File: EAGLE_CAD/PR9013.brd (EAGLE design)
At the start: 70.1 x 70.1 mm, 55 parts, among them J1 M3_SCREW_POST, SW1 SPST_TACT-KMR2, Y1 32.768kHz

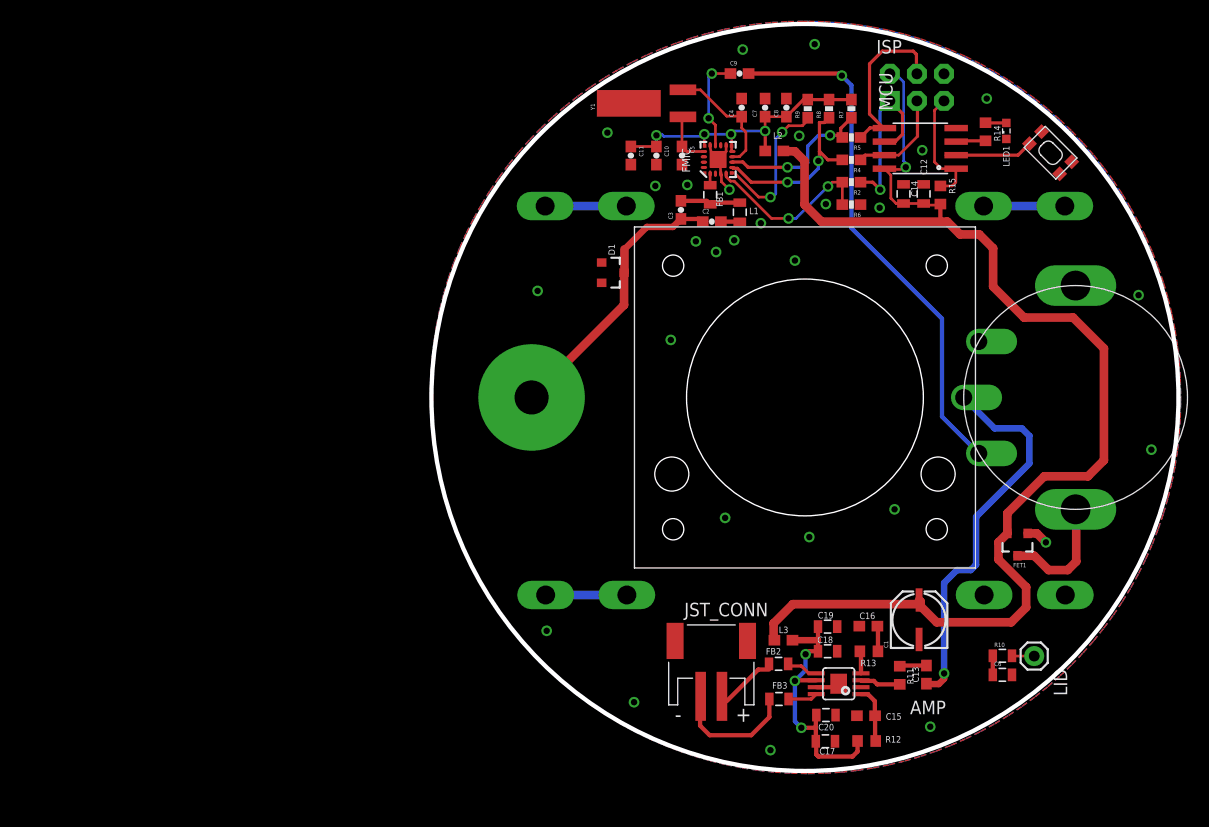
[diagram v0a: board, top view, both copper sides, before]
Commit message: Some significant fixes & changes
So i started by looking at the alignment of the board, speaker, pot &
antenna. it turns out these were all a bit wacky - all laid out at
different grid spacings and none of them consistent. the alignment of
all was off relative to one another, and the board itself was just at
some arbitrary location. so:

i moved the whole board so that it’s centered at 35mm x 35mm
moved the speaker so it’s centered at 35mm x 35mm
moved the antenna and pot so they’re centered at 35mm (Ydim) and are
each 25.5mm from centerline in the Xdim
moved the batteries so that they’re centered at 35mm (Xdim) and each
18.5mm from centerline in the Ydim

then i:
added a wire for the batteries on the left side. i’d like to modify
this but it’s a start.
added bRestrict circles for the four bolts for the speaker. these are
just over 5mm in diameter, so they’re just a little bigger than our
nuts will be. there should be NO TRACES IN THESE ZONES!!!

i did *NOT* remove all the traces in those bRestricts, though - i need
to do other stuff at the moment.

there MAY BE SOME OTHER CHANGES NECESSARY as a result of my
modifications. i wanted to get all the mechanical components 100% set
and locked, so that’s all i’m sure of at the minute.
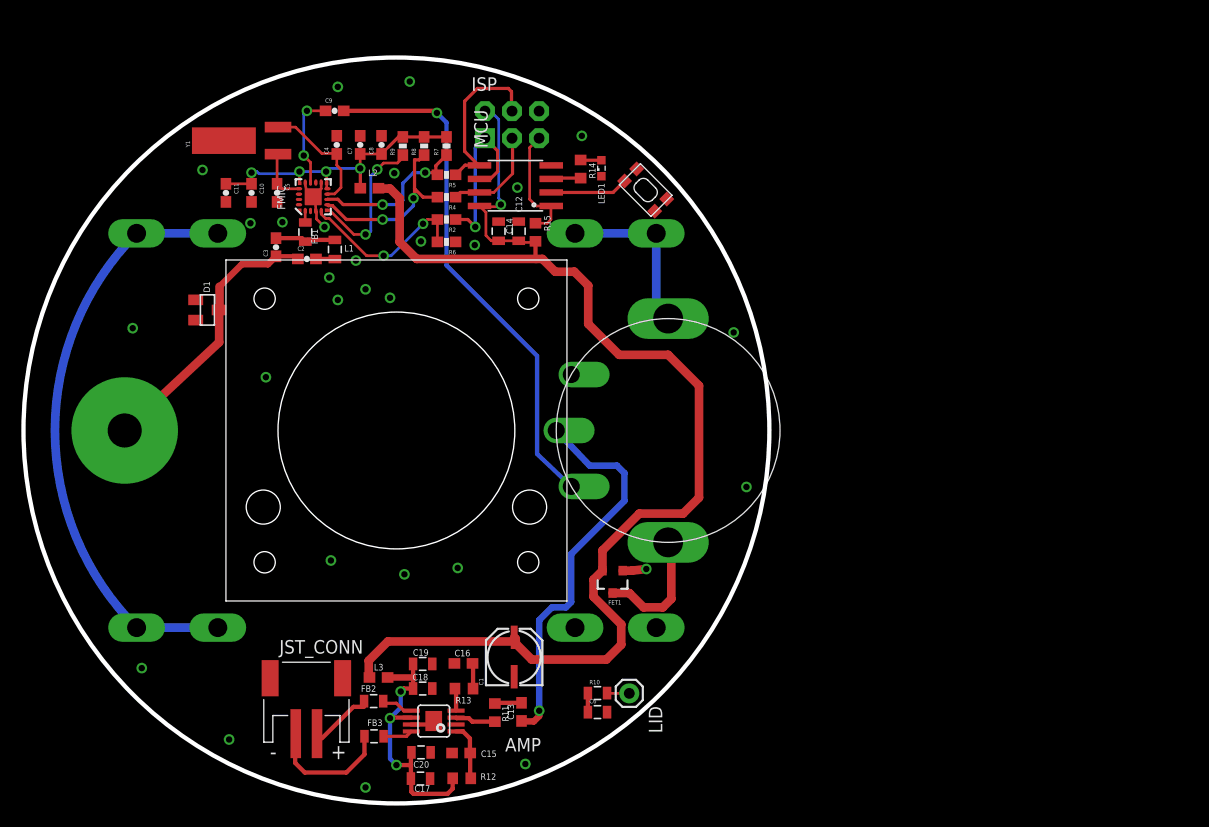
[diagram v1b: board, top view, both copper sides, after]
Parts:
- D1: device SparkFun-DiscreteSemi:SOT23-3 -> SparkFun-DiscreteSemi:SOT23
- moved JP6 38.5 mm to (35.0, 16.5)
- moved SPEAKER 38.5 mm to (35.0, 35.0)
- moved JP5 38.4 mm to (35.0, 53.5)
- moved R1 38.4 mm to (60.5, 35.0)
- moved J1 38.3 mm to (9.50, 35.0)
- moved C1 38.2 mm to (45.9, 13.7)
- moved C17 38.2 mm to (37.3, 2.33)
- moved C4 38.2 mm to (29.4, 61.8)
- moved FB2 38.2 mm to (32.9, 9.60)
- moved FB3 38.2 mm to (32.9, 6.30)
- moved AMP 38.2 mm to (38.5, 7.73)
- moved C10 38.2 mm to (21.4, 57.3)
- moved C11 38.2 mm to (19.0, 57.3)
- moved C12 38.2 mm to (46.5, 53.7)
- moved C14 38.2 mm to (44.6, 53.7)
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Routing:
- net N$13: track 15.2 -> 52.2 mm
- net N$15: track 7.62 -> 16.1 mm
- added copper zone on layer 16, net N$21
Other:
- board size 70.1 x 70.1 mm -> 70 x 70 mm

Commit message: moved some traces
redid left battery trace
redid the traces that were violating brestrict near the speaker
moved the lid connection off the board - think we’ll prob move that to
the speaker screws
moved other traces in small ways
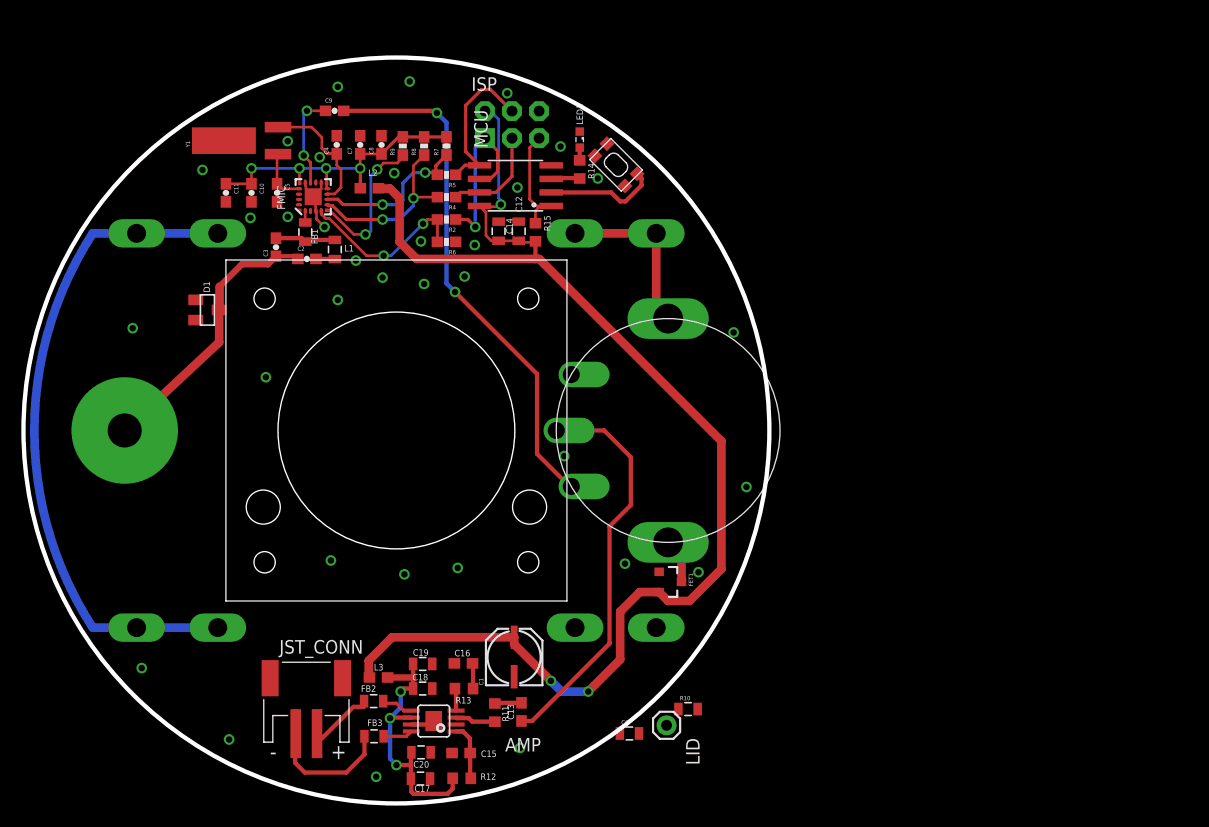
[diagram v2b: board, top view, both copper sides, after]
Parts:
- moved R10 8.63 mm to (62.4, 8.85)
- moved FET1 5.37 mm to (60.7, 20.8), turned to 270 degrees
- moved LID 4.61 mm to (60.4, 7.33)
- moved SW1 3.65 mm to (55.6, 59.9), turned to 315 degrees
- moved C6 3.61 mm to (56.9, 6.57)
- moved LED1 3.37 mm to (52.2, 62.3), turned to 270 degrees
- moved R14 0.10 mm to (52.2, 59.5)
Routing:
- net N$13: track 52.2 -> 60.5 mm
- net N$34: track 11.8 -> 4.23 mm
- net N$11: track 8.30 -> 11.7 mm
- net GND: track 13.6 -> 11.3 mm, vias 28 -> 34
- net N$8: track 2.10 -> 0.00 mm
- net N$35: track 1.79 -> 0.00 mm
- net SDIO: track 16.1 -> 14.6 mm
- net PB5: track 11.3 -> 10.2 mm
- net A_OUT: track 36.9 -> 37.6 mm, vias 1 -> 0
- net N$7: track 1.96 -> 1.20 mm
- net 3.3V: track 28.7 -> 29.4 mm
- net N$1: track 11.4 -> 12.0 mm
- net VCC: track 123.6 -> 124.1 mm, vias 1 -> 3
- net A_IN: vias 1 -> 2

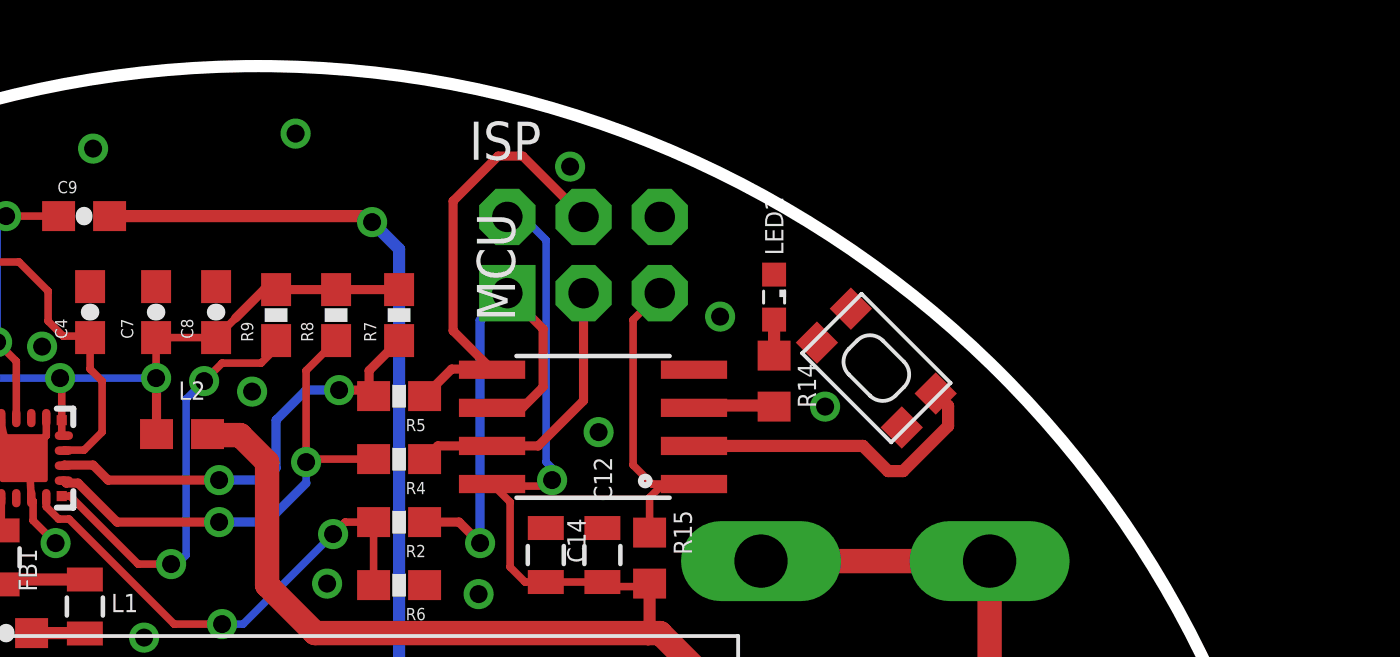
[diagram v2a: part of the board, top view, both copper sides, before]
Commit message: Updated Parts
Added the C&K part to PR Parts Library and updated PR9013 to include
this part.
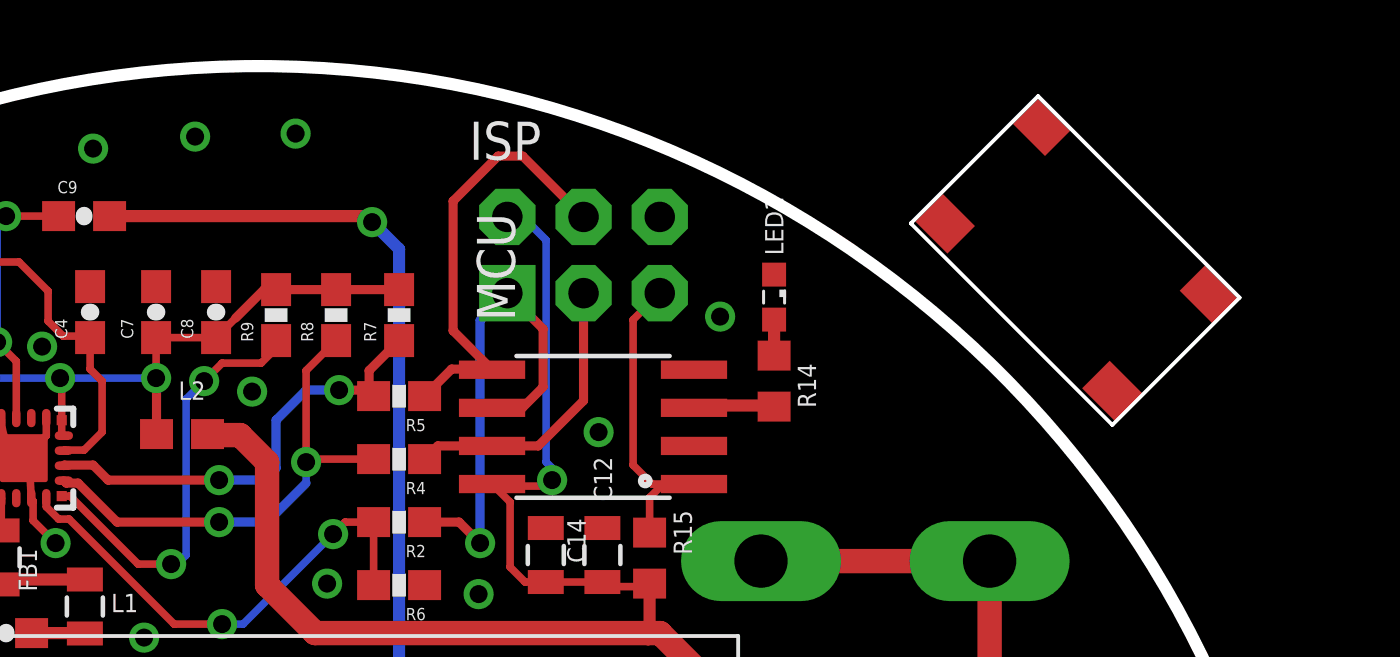
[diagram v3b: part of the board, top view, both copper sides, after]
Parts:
- removed SW1: SPST_TACT-KMR2, adafruit:KMR2
- added U$1: C&KPTS6465, PR_Parts_Library:C&K_TACTILE_SWITCH
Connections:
- net GND: now also U$1.P$1; no longer SW1.2
- net N$11: now also U$1.P$3; no longer SW1.1
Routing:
- net N$11: track 11.7 -> 0.97 mm
- net GND: vias 34 -> 33
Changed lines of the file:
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@@
 <attribute name="NAME" x="43.564" y="61.504" size="1.27" layer="25" rot="R90"/>
 </element>
-<element name="SW1" library="adafruit" package="KMR2" value="SPST_TACT-KMR2" x="55.608" y="59.934" smashed="yes" rot="R315"/>
 <element name="ISP" library="SparkFun-Connectors" package="2X3-NS" value="AVR_SPI_PRG_6NS" x="45.848" y="63.702" smashed="yes">
 <attribute name="NAME" x="42.038" y="66.877" size="1.27" layer="25" ratio="10"/>
@@
 <element name="C10" library="SparkFun-Passives" package="0603-CAP" value="" x="21.4" y="57.3" rot="R270"/>
 <element name="C11" library="SparkFun-Passives" package="0603-CAP" value="" x="19" y="57.3" rot="R270"/>
+<element name="U$1" library="PR_Parts_Library" package="C&amp;K_TACTILE_SWITCH" value="C&amp;KPTS6465" x="61" y="69" rot="R315"/>
 </elements>
 <signals>
@@
 <contactref element="FET1" pad="1"/>
 <contactref element="MCU" pad="4"/>
-<contactref element="SW1" pad="2"/>
 <contactref element="ISP" pad="6"/>
 <contactref element="LED1" pad="C"/>
@@
 <via x="63.35" y="21.7" extent="1-16" drill="0.6"/>
 <via x="50.75" y="32.6" extent="1-16" drill="0.6"/>
-<via x="53.9" y="58.65" extent="1-16" drill="0.6"/>
-<via x="45.4" y="66.65" extent="1-16" drill="0.6"/>
+<via x="32.9" y="67.65" extent="1-16" drill="0.6"/>
 <via x="27.8" y="60.65" extent="1-16" drill="0.6"/>
 <via x="24.8" y="62.15" extent="1-16" drill="0.6"/>
-<wire x1="27.19" y1="56.932" x2="27.2" y2="56.95" width="0" layer="19" extent="1-1"/>
+<contactref element="U$1" pad="P$1"/>
+<wire x1="66.65" y1="44.2" x2="61.14141875" y2="68.01005" width="0" layer="19" extent="1-1"/>
+<wire x1="27.2" y1="56.95" x2="27.19" y2="56.932" width="0" layer="19" extent="1-1"/>
 <wire x1="38.16" y1="2.332" x2="33.1" y2="2.5" width="0" layer="19" extent="1-1"/>
 <wire x1="57.768" y1="6.568" x2="59.384" y2="16.5" width="0" layer="19" extent="1-1"/>
@@
 <signal name="N$11">
 <contactref element="MCU" pad="2"/>
-<contactref element="SW1" pad="1"/>
 <wire x1="49.5302" y1="57.339" x2="48.561" y2="57.339" width="0.254" layer="1"/>
-<wire x1="49.5302" y1="57.339" x2="55.161" y2="57.339" width="0.4064" layer="1"/>
-<wire x1="55.161" y1="57.339" x2="56" y2="56.5" width="0.4064" layer="1"/>
-<wire x1="56" y1="56.5" x2="56.5" y2="56.5" width="0.4064" layer="1"/>
-<wire x1="56.5" y1="56.5" x2="58" y2="58" width="0.4064" layer="1"/>
-<wire x1="58" y1="58" x2="58" y2="58.673365625" width="0.4064" layer="1"/>
-<wire x1="58" y1="58.673365625" x2="57.587896875" y2="59.08546875" width="0.4064" layer="1"/>
+<contactref element="U$1" pad="P$3"/>
+<wire x1="49.5302" y1="57.339" x2="57.888728125" y2="64.75735625" width="0" layer="19" extent="1-1"/>
 </signal>
 <signal name="N$12">
